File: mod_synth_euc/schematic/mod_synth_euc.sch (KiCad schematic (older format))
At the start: 12 parts

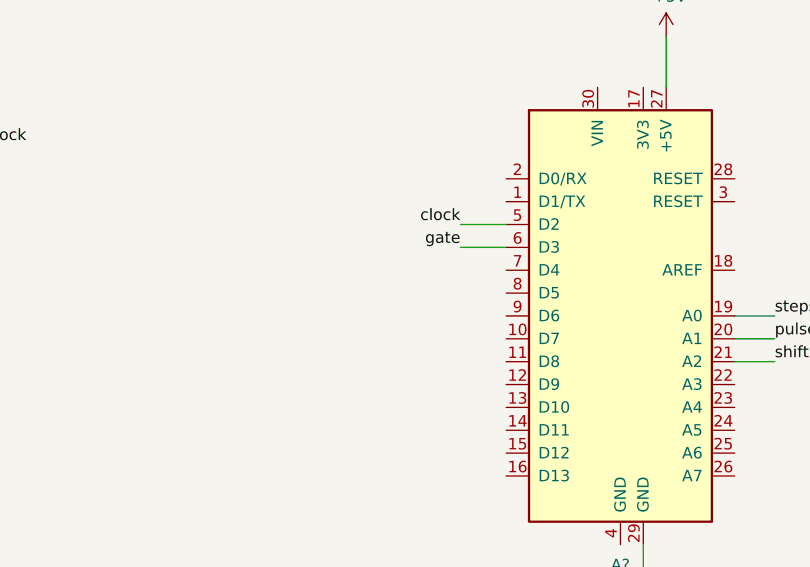
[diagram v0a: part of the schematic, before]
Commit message: Add indicator leds, update firmware to match schematic
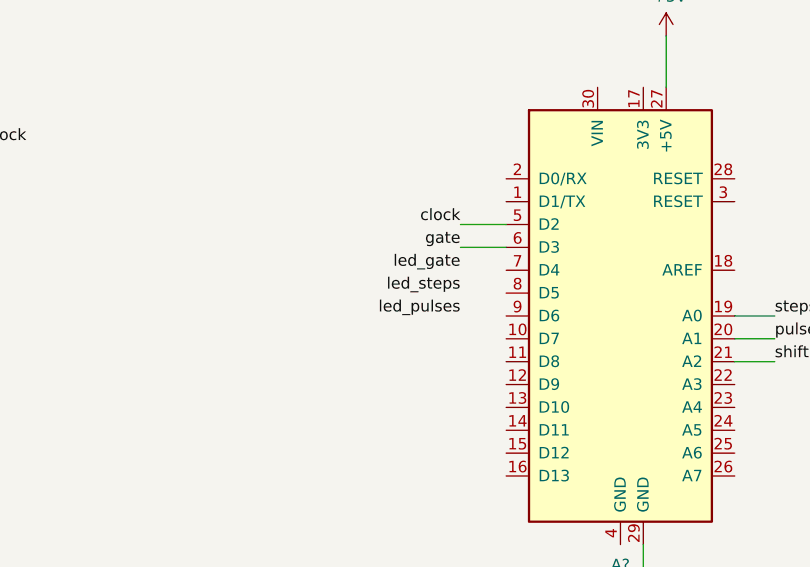
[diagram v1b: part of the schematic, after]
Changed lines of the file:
@@
 EESchema Schematic File Version 4
+LIBS:mod_synth_euc-cache
 EELAYER 29 0
 EELAYER END
@@
 Wire Wire Line
 	2725 1725 2850 1725
+Text Label 5425 2275 2    50   ~ 0
+led_gate
+Text Label 5425 2375 2    50   ~ 0
+led_steps
+Text Label 5425 2475 2    50   ~ 0
+led_pulses
 $EndSCHEMATC

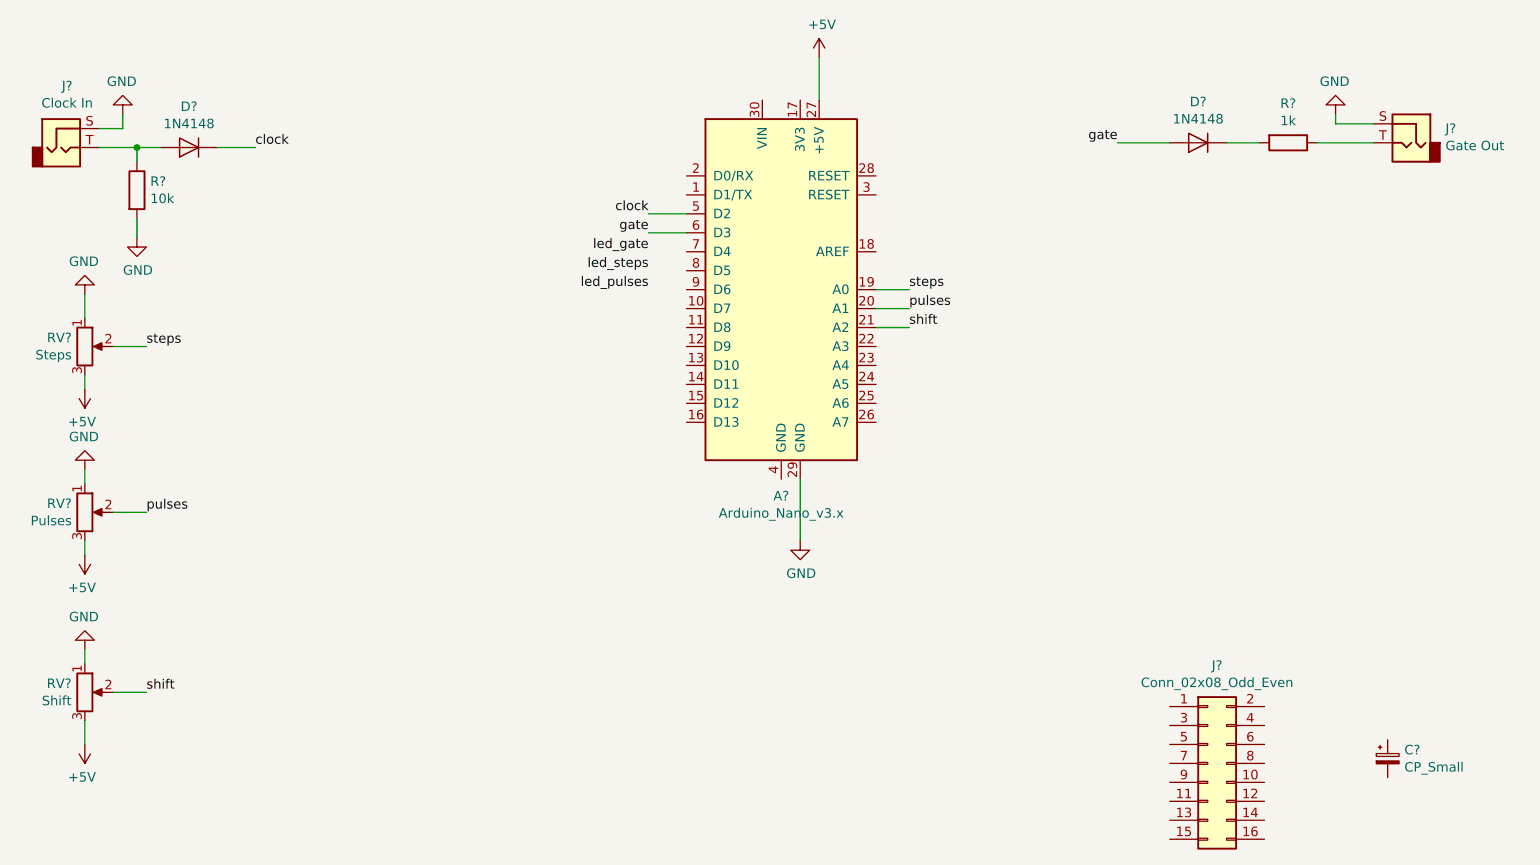
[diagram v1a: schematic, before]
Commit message: Attempt PCB layout for euclidean rhythms
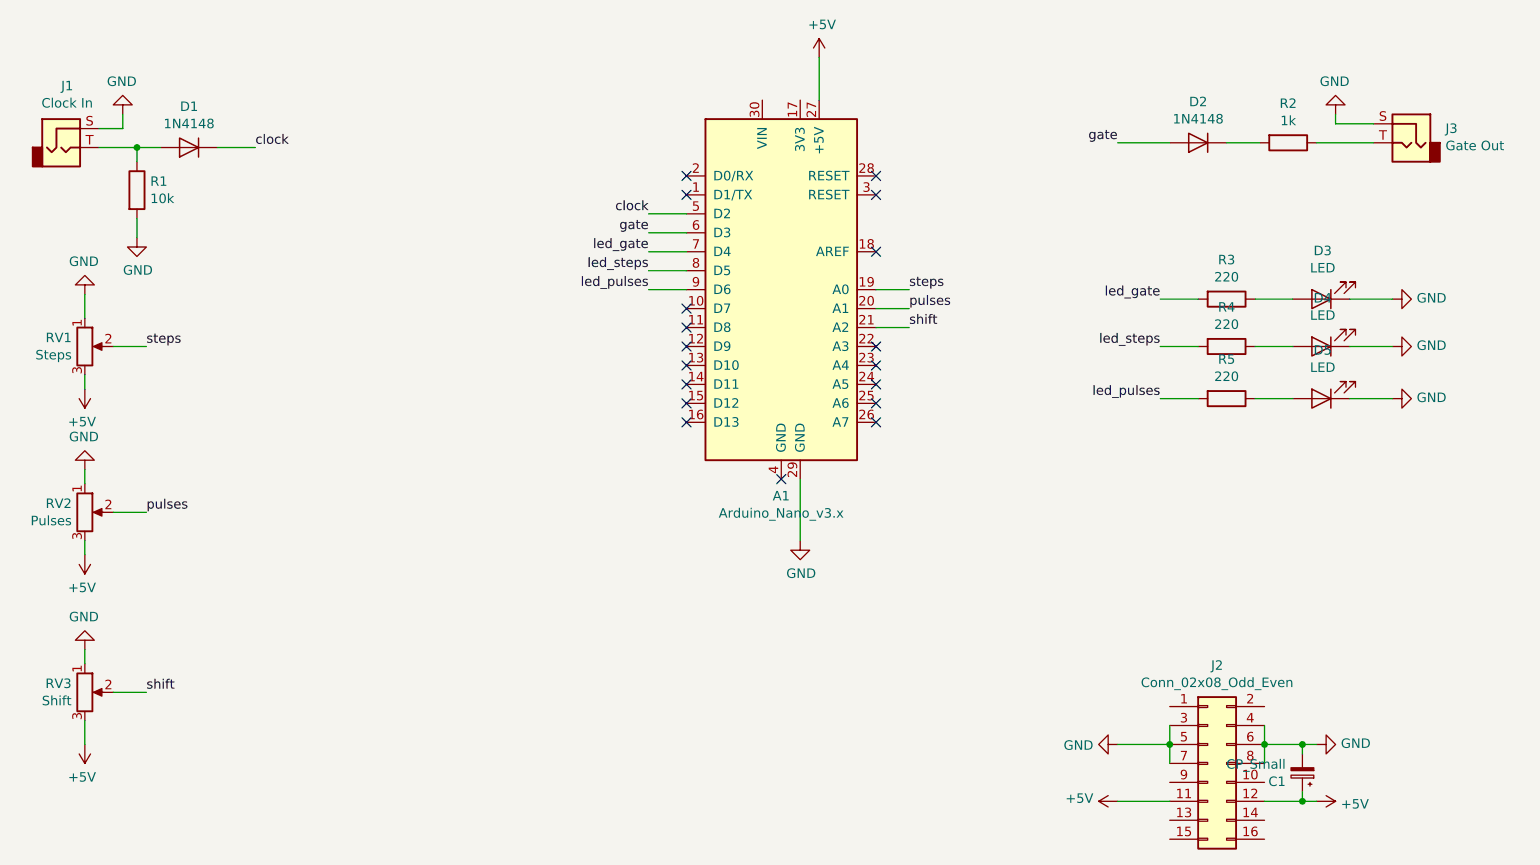
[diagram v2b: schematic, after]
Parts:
- added D3, D4, D5: LED, LED_THT:LED_D5.0mm, symbol Device:LED
- added R3, R4, R5: 220, Resistor_THT:R_Axial_DIN0207_L6.3mm_D2.5mm_P10.16mm_Horizontal, symbol Device:R
- C1: renamed from C?; footprint (none) -> Capacitor_THT:CP_Radial_D5.0mm_P2.00mm
- J1, J3: renamed from J?; footprint (none) -> Connector_Audio:Jack_3.5mm_QingPu_WQP-PJ398SM_Vertical_CircularHoles
- J2: renamed from J?; footprint (none) -> Connector_IDC:IDC-Header_2x08_P2.54mm_Vertical
- R1, R2: renamed from R?; footprint (none) -> Resistor_THT:R_Axial_DIN0207_L6.3mm_D2.5mm_P10.16mm_Horizontal
- RV1, RV2, RV3: renamed from RV?; footprint (none) -> Potentiometer_THT:Potentiometer_Alpha_RD901F-40-00D_Single_Vertical_CircularHoles
- gave numbers to parts that had none: 3
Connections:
- net +5V: now also C1.1, J2.11 (Pin_11), J2.12 (Pin_12)
- net GND: now also C1.2, J2.3 (Pin_3), J2.4 (Pin_4), J2.5 (Pin_5), J2.6 (Pin_6), J2.7 (Pin_7), J2.8 (Pin_8), D3.1 (K), D4.1 (K), D5.1 (K)
- net led_gate: now also A1.7 (D4), R3.2
- net led_pulses: now also A1.9 (D6), R5.2
- net led_steps: now also A1.8 (D5), R4.2
- new net: D3.2 (A), R3.1
- new net: D4.2 (A), R4.1
- new net: D5.2 (A), R5.1
- no-connect marks 0 -> 18
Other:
- moved on the sheet: C1

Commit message: Remove steps/pulses LEDs for one PCB
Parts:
- removed D4, D5: LED, LED_THT:LED_D5.0mm, symbol Device:LED
- removed R4, R5: 220, Resistor_THT:R_Axial_DIN0207_L6.3mm_D2.5mm_P10.16mm_Horizontal, symbol Device:R
- J2: value Conn_02x08_Odd_Even -> Conn_02x06_Odd_Even; footprint Connector_IDC:IDC-Header_2x08_P2.54mm_Vertical -> Connector_IDC:IDC-Header_2x06_P2.54mm_Vertical; symbol Connector_Generic:Conn_02x08_Odd_Even -> Connector_Generic:Conn_02x06_Odd_Even
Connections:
- net led_pulses: no longer names the net of A1.9 (D6)
- net led_steps: no longer names the net of A1.8 (D5)
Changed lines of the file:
@@
-$EndComp
-$Comp
-L Connector_Generic:Conn_02x08_Odd_Even J2
-U 1 1 5D6456BC
-P 8375 4975
-F 0 "J2" H 8425 5492 50  0000 C CNN
-F 1 "Conn_02x08_Odd_Even" H 8425 5401 50  0000 C CNN
-F 2 "Connector_IDC:IDC-Header_2x08_P2.54mm_Vertical" H 8375 4975 50  0001 C CNN
-F 3 "~" H 8375 4975 50  0001 C CNN
-	1    8375 4975
-	1    0    0    -1
 $EndComp
 $Comp
@@
 $EndComp
 $Comp
-L Device:CP_Small C1
-U 1 1 5D650349
-P 8875 5025
-F 0 "C1" H 8963 5071 50  0000 L CNN
-F 1 "CP_Small" H 8963 4980 50  0000 L CNN
-F 2 "Capacitor_THT:CP_Radial_D5.0mm_P2.00mm" H 8875 5025 50  0001 C CNN
-F 3 "~" H 8875 5025 50  0001 C CNN
-	1    8875 5025
-	-1   0    0    1
-$EndComp
-$Comp
 L power:+5V #PWR0110
 U 1 1 5D6519BB
@@
 Text Label 5425 2275 2    50   ~ 0
 led_gate
-Text Label 5425 2375 2    50   ~ 0
-led_steps
-Text Label 5425 2475 2    50   ~ 0
-led_pulses
 Wire Wire Line
 	8175 4775 8175 4875
@@
 	0    1    1    0
 $EndComp
-$Comp
-L power:GND #PWR0113
-U 1 1 5D653C19
-P 8950 4875
-F 0 "#PWR0113" H 8950 4625 50  0001 C CNN
-F 1 "GND" V 8955 4747 50  0000 R CNN
-F 2 "" H 8950 4875 50  0001 C CNN
-F 3 "" H 8950 4875 50  0001 C CNN
-	1    8950 4875
-	0    -1   -1   0
-$EndComp
-Wire Wire Line
-	8950 4875 8875 4875
 Wire Wire Line
 	8175 4875 7900 4875
@@
 	0    -1   -1   0
 $EndComp
-$Comp
-L power:+5V #PWR0115
-U 1 1 5D655317
-P 8950 5175
-F 0 "#PWR0115" H 8950 5025 50  0001 C CNN
-F 1 "+5V" V 8965 5303 50  0000 L CNN
-F 2 "" H 8950 5175 50  0001 C CNN
-F 3 "" H 8950 5175 50  0001 C CNN
-	1    8950 5175
-	0    1    1    0
-$EndComp
 Wire Wire Line
 	7900 5175 8175 5175
-Wire Wire Line
-	8950 5175 8875 5175
-Wire Wire Line
-	8875 4925 8875 4875
-Connection ~ 8875 4875
-Wire Wire Line
-	8875 4875 8675 4875
-Wire Wire Line
-	8875 5125 8875 5175
-Connection ~ 8875 5175
-Wire Wire Line
-	8875 5175 8675 5175
 NoConn ~ 6625 3175
 NoConn ~ 6625 3075
@@
 Wire Wire Line
 	5425 2275 5625 2275
-Wire Wire Line
-	5625 2375 5425 2375
-Wire Wire Line
-	5425 2475 5625 2475
 $Comp
 L Device:LED D3
@@
 F 3 "~" H 8975 2525 50  0001 C CNN
 	1    8975 2525
-	-1   0    0    1
-$EndComp
-$Comp
-L Device:LED D4
-U 1 1 5D66A6FF
-P 8975 2775
-F 0 "D4" H 8968 2520 50  0000 C CNN
-F 1 "LED" H 8968 2611 50  0000 C CNN
-F 2 "LED_THT:LED_D5.0mm" H 8975 2775 50  0001 C CNN
-F 3 "~" H 8975 2775 50  0001 C CNN
-	1    8975 2775
-	-1   0    0    1
-$EndComp
-$Comp
-L Device:LED D5
-U 1 1 5D66A9E5
-P 8975 3050
-F 0 "D5" H 8968 2795 50  0000 C CNN
-F 1 "LED" H 8968 2886 50  0000 C CNN
-F 2 "LED_THT:LED_D5.0mm" H 8975 3050 50  0001 C CNN
-F 3 "~" H 8975 3050 50  0001 C CNN
-	1    8975 3050
 	-1   0    0    1
 $EndComp
@@
 	0    -1   -1   0
 $EndComp
-$Comp
-L power:GND #PWR0117
-U 1 1 5D66B8E9
-P 9350 2775
-F 0 "#PWR0117" H 9350 2525 50  0001 C CNN
-F 1 "GND" V 9355 2647 50  0000 R CNN
-F 2 "" H 9350 2775 50  0001 C CNN
-F 3 "" H 9350 2775 50  0001 C CNN
-	1    9350 2775
-	0    -1   -1   0
-$EndComp
-$Comp
-L power:GND #PWR0118
-U 1 1 5D66BC0D
-P 9350 3050
-F 0 "#PWR0118" H 9350 2800 50  0001 C CNN
-F 1 "GND" V 9355 2922 50  0000 R CNN
-F 2 "" H 9350 3050 50  0001 C CNN
-F 3 "" H 9350 3050 50  0001 C CNN
-	1    9350 3050
-	0    -1   -1   0
-$EndComp
 Wire Wire Line
 	9125 2525 9350 2525
-Wire Wire Line
-	9350 2775 9125 2775
-Wire Wire Line
-	9125 3050 9350 3050
 $Comp
 L Device:R R3
@@
 	0    1    1    0
 $EndComp
-$Comp
-L Device:R R4
-U 1 1 5D66E15D
-P 8475 2775
-F 0 "R4" V 8268 2775 50  0000 C CNN
-F 1 "220" V 8359 2775 50  0000 C CNN
-F 2 "Resistor_THT:R_Axial_DIN0207_L6.3mm_D2.5mm_P10.16mm_Horizontal" V 8405 2775 50  0001 C CNN
-F 3 "~" H 8475 2775 50  0001 C CNN
-	1    8475 2775
-	0    1    1    0
-$EndComp
-$Comp
-L Device:R R5
-U 1 1 5D66E426
-P 8475 3050
-F 0 "R5" V 8268 3050 50  0000 C CNN
-F 1 "220" V 8359 3050 50  0000 C CNN
-F 2 "Resistor_THT:R_Axial_DIN0207_L6.3mm_D2.5mm_P10.16mm_Horizontal" V 8405 3050 50  0001 C CNN
-F 3 "~" H 8475 3050 50  0001 C CNN
-	1    8475 3050
-	0    1    1    0
-$EndComp
 Wire Wire Line
 	8625 2525 8825 2525
-Wire Wire Line
-	8825 2775 8625 2775
-Wire Wire Line
-	8625 3050 8825 3050
 Text Label 8125 2525 2    50   ~ 0
 led_gate
-Text Label 8125 2775 2    50   ~ 0
-led_steps
-Text Label 8125 3050 2    50   ~ 0
-led_pulses
 Wire Wire Line
 	8125 2525 8325 2525
-Wire Wire Line
-	8325 2775 8125 2775
-Wire Wire Line
-	8125 3050 8325 3050
+$Comp
+L Connector_Generic:Conn_02x06_Odd_Even J2
+U 1 1 5D6456BC
+P 8375 4875
+F 0 "J2" H 8425 5392 50  0000 C CNN
+F 1 "Conn_02x06_Odd_Even" H 8425 5301 50  0000 C CNN
+F 2 "Connector_IDC:IDC-Header_2x06_P2.54mm_Vertical" H 8375 4875 50  0001 C CNN
+F 3 "~" H 8375 4875 50  0001 C CNN
+	1    8375 4875
+	1    0    0    -1
+$EndComp
+Wire Wire Line
+	8875 5175 8675 5175
+Connection ~ 8875 5175
+Wire Wire Line
+	8875 5125 8875 5175
+Wire Wire Line
+	8875 4875 8675 4875
+Connection ~ 8875 4875
+Wire Wire Line
+	8875 4925 8875 4875
+Wire Wire Line
+	8950 5175 8875 5175
+$Comp
+L power:+5V #PWR0115
+U 1 1 5D655317
+P 8950 5175
+F 0 "#PWR0115" H 8950 5025 50  0001 C CNN
+F 1 "+5V" V 8965 5303 50  0000 L CNN
+F 2 "" H 8950 5175 50  0001 C CNN
+F 3 "" H 8950 5175 50  0001 C CNN
+	1    8950 5175
+	0    1    1    0
+$EndComp
+Wire Wire Line
+	8950 4875 8875 4875
+$Comp
+L power:GND #PWR0113
+U 1 1 5D653C19
+P 8950 4875
+F 0 "#PWR0113" H 8950 4625 50  0001 C CNN
+F 1 "GND" V 8955 4747 50  0000 R CNN
+F 2 "" H 8950 4875 50  0001 C CNN
+F 3 "" H 8950 4875 50  0001 C CNN
+	1    8950 4875
+	0    -1   -1   0
+$EndComp
+$Comp
+L Device:CP_Small C1
+U 1 1 5D650349
+P 8875 5025
+F 0 "C1" H 8963 5071 50  0000 L CNN
+F 1 "CP_Small" H 8963 4980 50  0000 L CNN
+F 2 "Capacitor_THT:CP_Radial_D5.0mm_P2.00mm" H 8875 5025 50  0001 C CNN
+F 3 "~" H 8875 5025 50  0001 C CNN
+	1    8875 5025
+	-1   0    0    1
+$EndComp
 $EndSCHEMATC

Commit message: Update ignore values, change connector on euclid
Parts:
- J2: value Conn_02x06_Odd_Even -> Conn_02x07_Odd_Even; footprint Connector_IDC:IDC-Header_2x06_P2.54mm_Vertical -> Connector_IDC:IDC-Header_2x07_P2.54mm_Vertical; symbol Connector_Generic:Conn_02x06_Odd_Even -> Connector_Generic:Conn_02x07_Odd_Even
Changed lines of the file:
@@
 	8125 2525 8325 2525
 $Comp
-L Connector_Generic:Conn_02x06_Odd_Even J2
+L Connector_Generic:Conn_02x07_Odd_Even J2
 U 1 1 5D6456BC
-P 8375 4875
-F 0 "J2" H 8425 5392 50  0000 C CNN
-F 1 "Conn_02x06_Odd_Even" H 8425 5301 50  0000 C CNN
-F 2 "Connector_IDC:IDC-Header_2x06_P2.54mm_Vertical" H 8375 4875 50  0001 C CNN
-F 3 "~" H 8375 4875 50  0001 C CNN
-	1    8375 4875
+P 8375 4975
+F 0 "J2" H 8425 5492 50  0000 C CNN
+F 1 "Conn_02x07_Odd_Even" H 8425 5401 50  0000 C CNN
+F 2 "Connector_IDC:IDC-Header_2x07_P2.54mm_Vertical" H 8375 4975 50  0001 C CNN
+F 3 "~" H 8375 4975 50  0001 C CNN
+	1    8375 4975
 	1    0    0    -1
 $EndComp

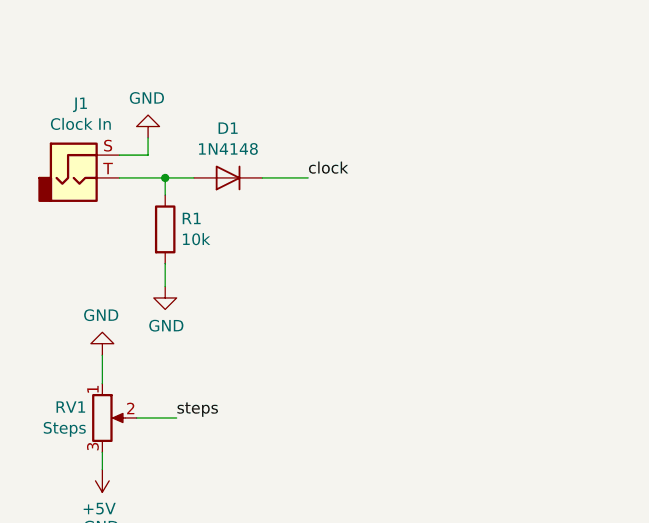
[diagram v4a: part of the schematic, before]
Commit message: Update resistor options
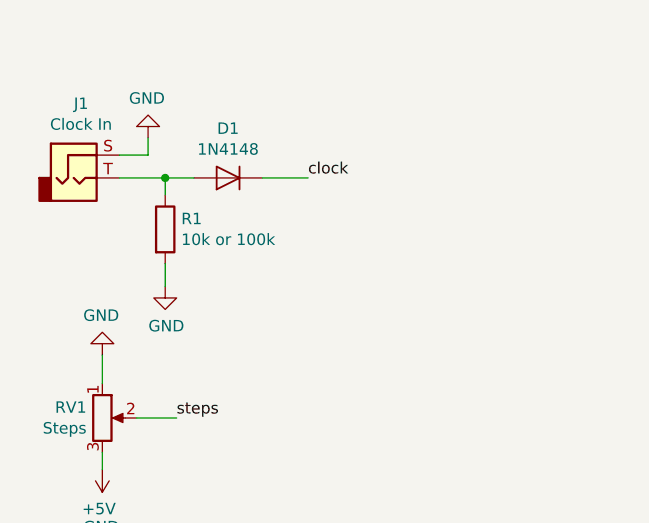
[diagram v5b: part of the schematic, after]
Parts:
- R1: value 10k -> 10k or 100k
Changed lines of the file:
@@
 P 2725 1950
 F 0 "R1" H 2795 1996 50  0000 L CNN
-F 1 "10k" H 2795 1905 50  0000 L CNN
+F 1 "10k or 100k" H 2795 1905 50  0000 L CNN
 F 2 "Resistor_THT:R_Axial_DIN0207_L6.3mm_D2.5mm_P10.16mm_Horizontal" V 2655 1950 50  0001 C CNN
 F 3 "~" H 2725 1950 50  0001 C CNN
